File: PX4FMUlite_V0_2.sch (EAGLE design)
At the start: 156 parts, among them J201 DF13C-6P-1.25V, J202 DF13C-6P-1.25V, J203 DF13C-6P-1.25V, J204 DF13C-6P-1.25V, J301 47346-0001, J302 DF13C-4P-1.25V, J401 DF13C-4P-1.25V, J403 DF13C-7P-1.25V, J404 DF13C-5P-1.25V, J405 DF13C-4P-1.25V, J702 DF13C-3P-1.25V, J801 JST-ZH-3, M3_MOUNT1101 MOUNT-HOLE3.1MM, M3_MOUNT1102 MOUNT-HOLE3.1MM, M3_MOUNT1103 MOUNT-HOLE3.1MM, M3_MOUNT1104 MOUNT-HOLE3.1MM, U1 MPU-6000QFN-24, U101 STM32F4X7VX, U102 FM25V01, U401 MAX3051, U701 TCA62724FMG, U703 LRTB GFTG-T7AW-1+V7A7-29+R5T9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, U903 74LVC2G240, X101 3.2x2.5 mm / 24 MHz / 15 ppm

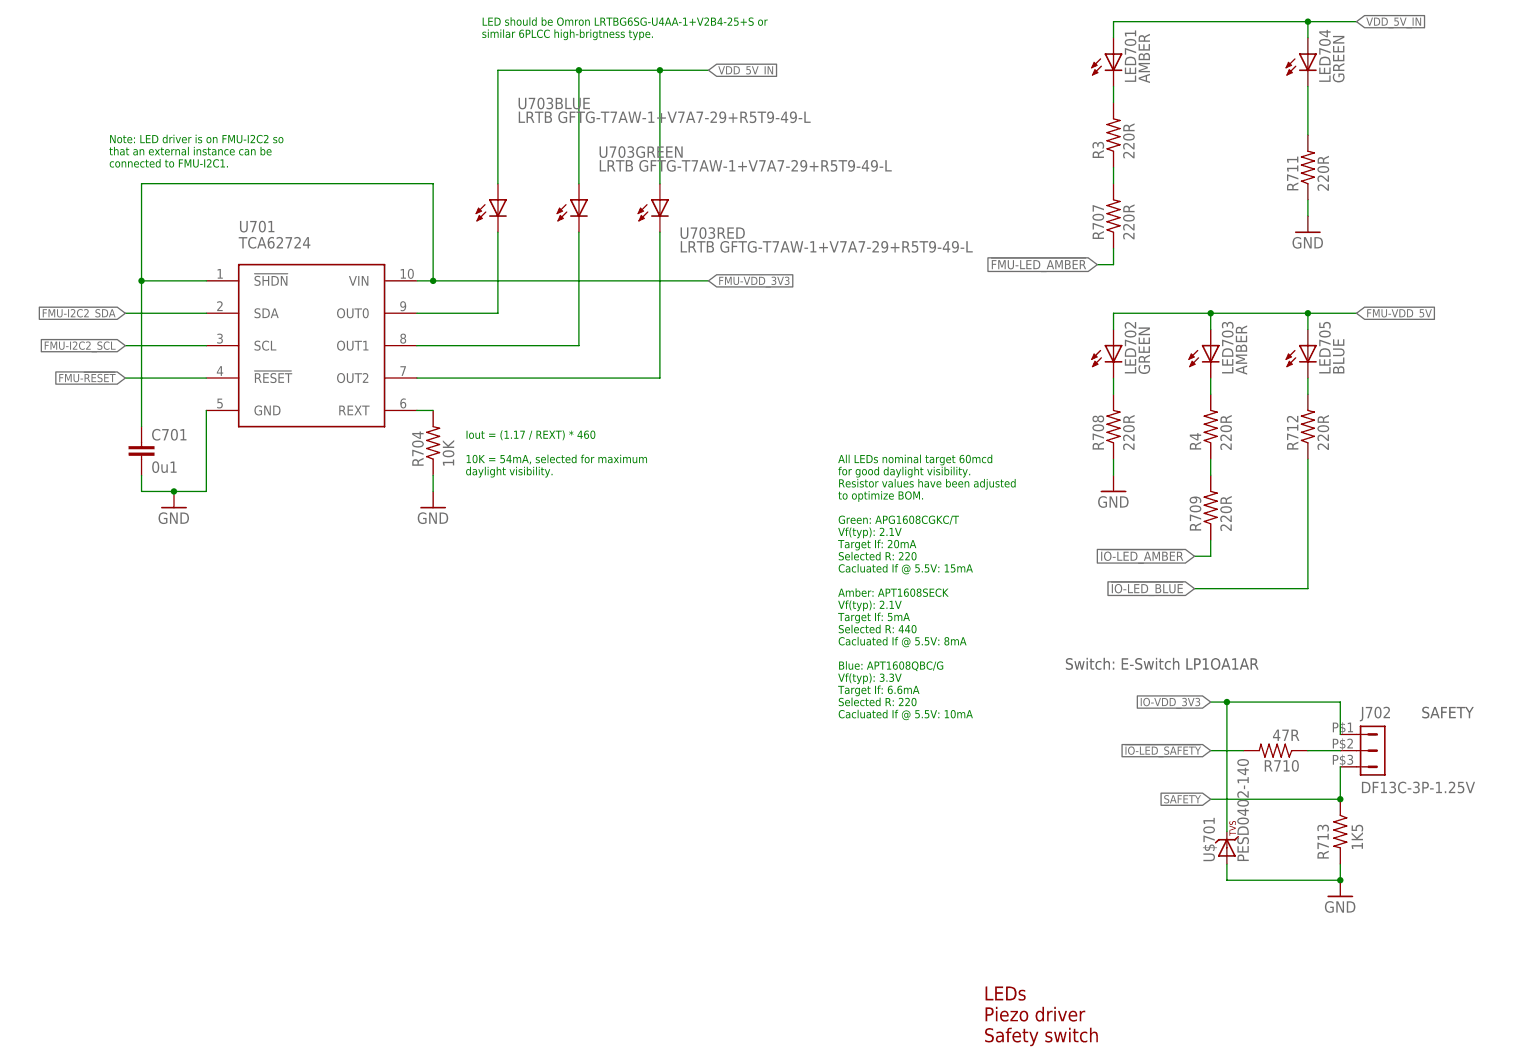
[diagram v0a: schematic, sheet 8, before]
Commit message: Added V0_2 because V0_1 would not save
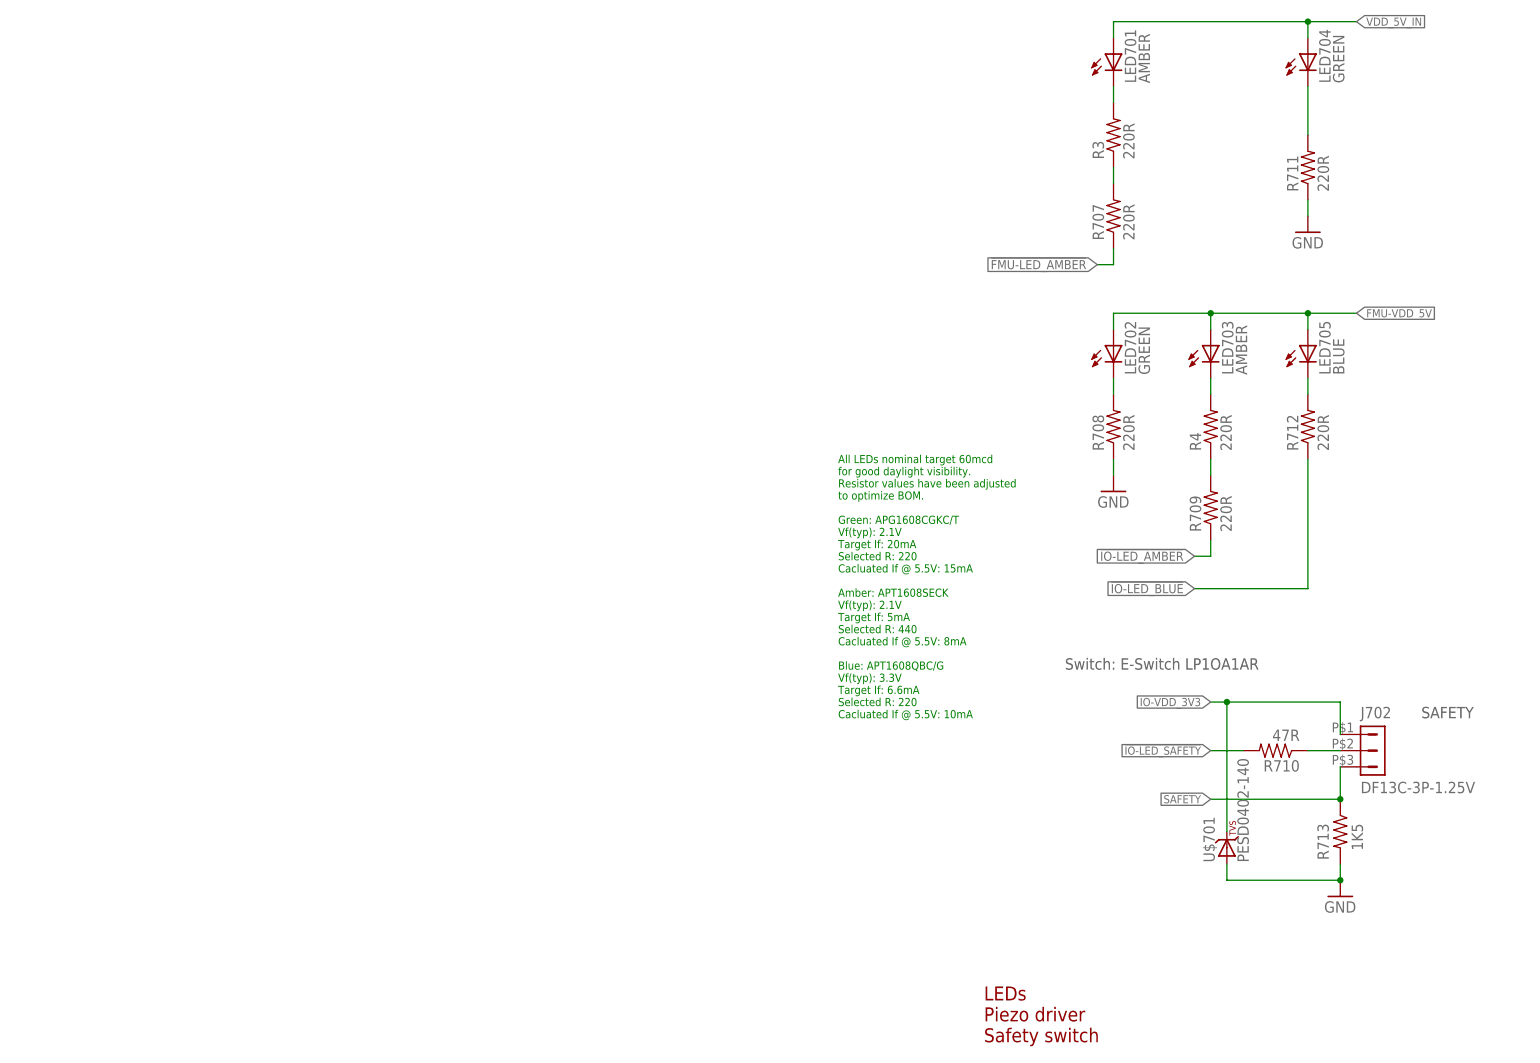
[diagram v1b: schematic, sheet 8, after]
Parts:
- removed C701: 0u1, pixhawk2:CAP0402
- removed L601, L602: KNH16C104DA5TS, pixhawk2:KNH16C104DA5TS
- removed R604, R605: 10K/0.1%, pixhawk2:RESISTOR0402-RES
- removed R704: 10K, pixhawk2:RESISTOR0402-RES
- removed U701: TCA62724FMG, pixhawk2:TCA62724FMG
- removed U703: LRTB GFTG-T7AW-1+V7A7-29+R5T9-49-L, pixhawk2:RGB-LED6-PLCC
- added U$2: LSM303D, PX4FMUlite_V0_1:LSM303D
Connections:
- removed net BATT_CURRENT_SENS: R604.1
- removed net BATT_VOLTAGE_SENS: R605.1
- removed net BATT_VOLTAGE_SENS_PROT: L602.P$1
- removed net N$102: L602.P$2, R605.2
- removed net N$103: L601.P$2, R604.2
- removed net N$21: L601.P$1
- removed net N$95: R704.2, U701.REXT
- removed net RGB_LED_14: U701.OUT2, U703RED.C
- removed net RGB_LED_3: U701.OUT0, U703BLUE.C
- removed net RGB_LED_4: U701.OUT1, U703GREEN.C
- net !ACCEL_MAG_CS: now also U$2.CS
- net ACCEL_DRDY: now also U$2.INT1
- net FMU-!RESET: no longer U701.!RESET
- net FMU-I2C2_SCL: no longer U701.SCL
- net FMU-I2C2_SDA: no longer U701.SDA
- net FMU-VDD_3V3: no longer C701.1, U701.!SHDN, U701.VIN
- net GNDX: now also U$2.GND@1, U$2.GND@2, U$2.GND@3, U$2.GND@4, U$2.RSRV; no longer C701.2, L601.P$3, L602.P$3, R704.1, U701.GND
- net MAG_DRDY: now also U$2.INT2
- net N$10: now also U$2.SETC
- net N$17: now also U$2.SETP
- net N$6: now also U$2.C1
- net SPI_INT_MISO: now also U$2.SDO/SA0
- net SPI_INT_MOSI: now also U$2.SDA/SDI/SDO
- net SPI_INT_SCK: now also U$2.SCL/SPC
- net VDD_3V3_SENSORS: now also U$2.VDD, U$2.VDD_IO
- net VDD_5V_IN: no longer U703BLUE.A, U703GREEN.A, U703RED.A
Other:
- note removed: "Iout = (1.17 / REXT) * 460 10K = 54mA, selected for maximum daylight visibility."
- note removed: "LED should be Omron LRTBG6SG-U4AA-1+V2B4-25+S or similar 6PLCC high-brigtness type."
- note removed: "Note: LED driver is on FMU-I2C2 so that an external instance can be connected to FMU-I2C1."

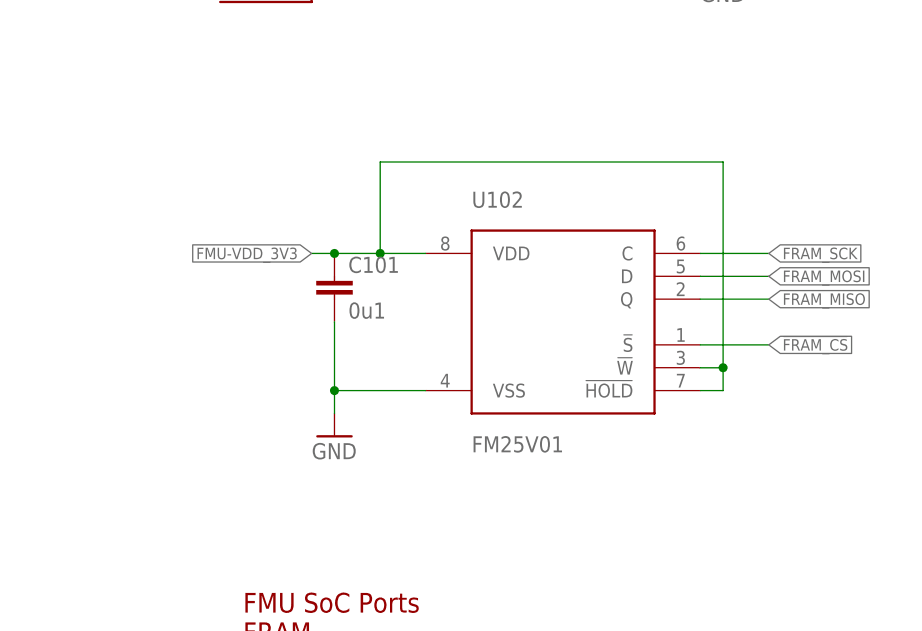
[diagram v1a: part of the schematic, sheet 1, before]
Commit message: Changed to winbond W25Q64 64mbit flash in 5*6 8WSON
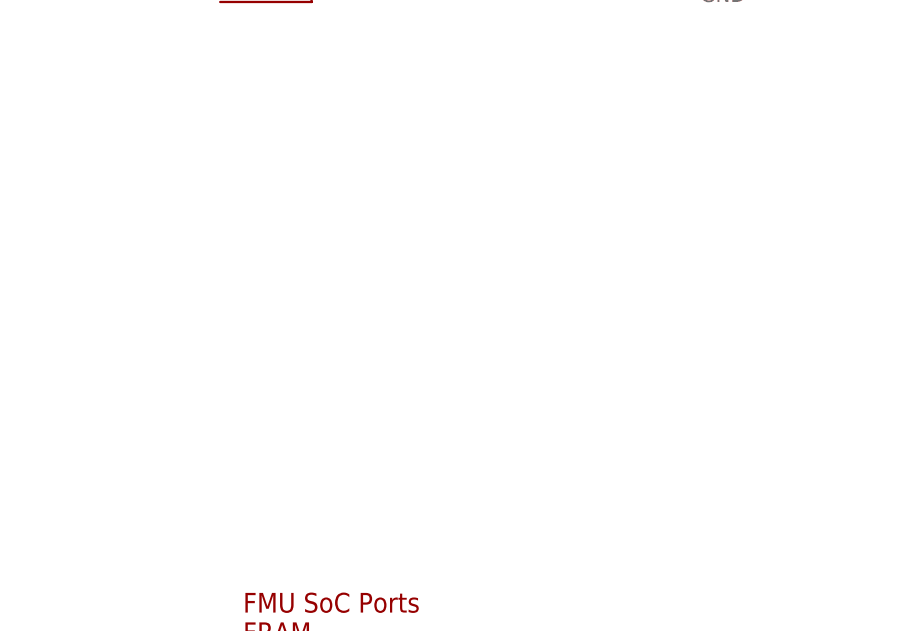
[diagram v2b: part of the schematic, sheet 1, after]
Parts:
- removed C101: 0u1, pixhawk2:CAP0402
- removed U102: FM25V01, pixhawk2:FM25V01
- added U$3: W25Q64FV, PX4lite:W25Q64FV
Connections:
- net !FRAM_CS: no longer U102.!S
- net FMU-VDD_3V3: no longer C101.1, U102.!HOLD, U102.!W, U102.VDD
- net FRAM_MISO: no longer U102.Q
- net FRAM_MOSI: no longer U102.D
- net FRAM_SCK: no longer U102.C
- net GNDX: no longer C101.2, U102.VSS
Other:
- note removed: "Stuff option 2: L3GD20H (replacement gyro)"
- note removed: "Stuff option 4: onboard accel/mag"
- note removed: "Valid stuff option combos: 1 + 4 2 + 4 3 only DO NOT stuff 1 + 2 at the same time DO NOT stuff 3 with any of 1, 2 or 4"
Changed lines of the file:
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@@
 <attribute name="PARTNO" value="RC0402FR-071K5L"/>
-</part>
-<part name="GND15" library="pixhawk2" deviceset="GND" device=""/>
-<part name="U102" library="pixhawk2" deviceset="FM25V01" device="">
-<attribute name="PARTNO" value="FM25V01-G"/>
-</part>
-<part name="C101" library="pixhawk2" deviceset="CAP" device="0402" value="0u1">
-<attribute name="PARTNO" value="CC0402ZRY5V7BB104"/>
 </part>
 <part name="J302" library="con-hirose-df13" deviceset="DF13-4P-1.25" device="V" value="DF13C-4P-1.25V">
@@
 <part name="U1" library="SparkFun-Sensors" deviceset="MPU-6000" device="QFN-24"/>
 <part name="U$2" library="PX4FMUlite_V0_1" deviceset="LSM303D" device=""/>
+<part name="U$3" library="PX4lite" deviceset="W25Q64FV" device=""/>
 </parts>
 <sheets>
@@
 <instance part="U101" gate="PORTE_H" x="165.1" y="129.54" rot="MR0"/>
 <instance part="U101" gate="OSC" x="165.1" y="91.44"/>
-<instance part="GND15" gate="1" x="172.72" y="38.1"/>
-<instance part="U102" gate="G$1" x="198.12" y="50.8">
-<attribute name="PARTNO" x="198.12" y="50.8" size="1.778" layer="96" display="off"/>
-</instance>
-<instance part="C101" gate="G$1" x="172.72" y="53.34">
-<attribute name="PARTNO" x="172.72" y="53.34" size="1.778" layer="96" display="off"/>
-</instance>
 <instance part="R101" gate="G$1" x="60.96" y="132.08">
 <attribute name="PARTNO" x="60.96" y="132.08" size="1.778" layer="96" display="off"/>
@@
 <pinref part="X101" gate="G$1" pin="NC_2"/>
 </segment>
-<segment>
-<pinref part="U102" gate="G$1" pin="VSS"/>
-<pinref part="GND15" gate="1" pin="GND"/>
-<wire x1="182.88" y1="43.18" x2="172.72" y2="43.18" width="0.1524" layer="91"/>
-<wire x1="172.72" y1="43.18" x2="172.72" y2="40.64" width="0.1524" layer="91"/>
-<pinref part="C101" gate="G$1" pin="2"/>
-<wire x1="172.72" y1="43.18" x2="172.72" y2="50.8" width="0.1524" layer="91"/>
-<junction x="172.72" y="43.18"/>
-</segment>
 </net>
 <net name="CAN1_RX" class="0">
@@
 </segment>
 </net>
-<net name="FMU-VDD_3V3" class="1">
-<segment>
-<pinref part="U102" gate="G$1" pin="VDD"/>
-<wire x1="182.88" y1="58.42" x2="177.8" y2="58.42" width="0.1524" layer="91"/>
-<label x="170.18" y="58.42" size="1.27" layer="95" rot="R180" xref="yes"/>
-<pinref part="C101" gate="G$1" pin="1"/>
-<wire x1="177.8" y1="58.42" x2="172.72" y2="58.42" width="0.1524" layer="91"/>
-<wire x1="172.72" y1="58.42" x2="170.18" y2="58.42" width="0.1524" layer="91"/>
-<junction x="172.72" y="58.42"/>
-<pinref part="U102" gate="G$1" pin="!HOLD"/>
-<wire x1="213.36" y1="43.18" x2="215.9" y2="43.18" width="0.1524" layer="91"/>
-<wire x1="215.9" y1="43.18" x2="215.9" y2="45.72" width="0.1524" layer="91"/>
-<wire x1="215.9" y1="45.72" x2="215.9" y2="68.58" width="0.1524" layer="91"/>
-<wire x1="215.9" y1="68.58" x2="177.8" y2="68.58" width="0.1524" layer="91"/>
-<wire x1="177.8" y1="68.58" x2="177.8" y2="58.42" width="0.1524" layer="91"/>
-<junction x="177.8" y="58.42"/>
-<pinref part="U102" gate="G$1" pin="!W"/>
-<wire x1="213.36" y1="45.72" x2="215.9" y2="45.72" width="0.1524" layer="91"/>
-<junction x="215.9" y="45.72"/>
-</segment>
-</net>
 <net name="!FRAM_CS" class="0">
-<segment>
-<pinref part="U102" gate="G$1" pin="!S"/>
-<wire x1="213.36" y1="48.26" x2="220.98" y2="48.26" width="0.1524" layer="91"/>
-<label x="220.98" y="48.26" size="1.27" layer="95" xref="yes"/>
-</segment>
 <segment>
 <pinref part="U101" gate="PORTD_H" pin="PD10"/>
@@
 <net name="FRAM_SCK" class="0">
 <segment>
-<pinref part="U102" gate="G$1" pin="C"/>
-<wire x1="213.36" y1="58.42" x2="220.98" y2="58.42" width="0.1524" layer="91"/>
-<label x="220.98" y="58.42" size="1.27" layer="95" xref="yes"/>
-</segment>
-<segment>
 <pinref part="U101" gate="PORTB_H" pin="PB13"/>
 <wire x1="33.02" y1="68.58" x2="38.1" y2="68.58" width="0.1524" layer="91"/>
@@
 <net name="FRAM_MOSI" class="0">
 <segment>
-<pinref part="U102" gate="G$1" pin="D"/>
-<wire x1="213.36" y1="55.88" x2="220.98" y2="55.88" width="0.1524" layer="91"/>
-<label x="220.98" y="55.88" size="1.27" layer="95" xref="yes"/>
-</segment>
-<segment>
 <pinref part="U101" gate="PORTB_H" pin="PB15"/>
 <wire x1="33.02" y1="63.5" x2="38.1" y2="63.5" width="0.1524" layer="91"/>
@@
 </net>
 <net name="FRAM_MISO" class="0">
-<segment>
-<pinref part="U102" gate="G$1" pin="Q"/>
-<wire x1="213.36" y1="53.34" x2="220.98" y2="53.34" width="0.1524" layer="91"/>
-<label x="220.98" y="53.34" size="1.27" layer="95" xref="yes"/>
-</segment>
 <segment>
 <pinref part="U101" gate="PORTB_H" pin="PB14"/>
@@
 <attribute name="PARTNO" x="53.34" y="134.62" size="1.778" layer="96" display="off"/>
 </instance>
+<instance part="U$3" gate="G$1" x="109.22" y="76.2"/>
 </instances>
 <busses>
@@
 <wire x1="248.92" y1="33.02" x2="185.42" y2="33.02" width="0.1524" layer="94" style="dashdot"/>
 <wire x1="185.42" y1="33.02" x2="185.42" y2="68.58" width="0.1524" layer="94" style="dashdot"/>
-<text x="6.35" y="34.29" size="1.778" layer="94">Stuff option 2: L3GD20H (replacement gyro)</text>
 <text x="187.198" y="34.036" size="1.778" layer="94">Stuff option 3: offboard gyro/accel/mag</text>
 <wire x1="127" y1="165.1" x2="254" y2="165.1" width="0.1524" layer="94" style="dashdot"/>
 <wire x1="254" y1="165.1" x2="254" y2="101.6" width="0.1524" layer="94" style="dashdot"/>
 <wire x1="254" y1="101.6" x2="127" y2="101.6" width="0.1524" layer="94" style="dashdot"/>
-<text x="128.016" y="102.616" size="1.778" layer="94">Stuff option 4: onboard accel/mag</text>
-<text x="101.6" y="10.16" size="1.778" layer="94">Valid stuff option combos:
-  1 + 4
-  2 + 4
-  3 only
-DO NOT stuff 1 + 2 at the same time
-DO NOT stuff 3 with any of 1, 2 or 4</text>
 <text x="22.86" y="111.76" size="1.778" layer="91">THIS IS A SPARKFUN LIBRARY PART USED FOR REFERENCE ONLY.
 MUST BE REPLACED WITH OWN LIBRARY PART</text>

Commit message: Test positioning
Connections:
- new net GND: U$3.GND
- net FMU-VDD_3V3: now also U$3.VCC
- net SDIO_CK: now also U$3.CLK
- net SDIO_CMD: now also U$3.!CS
- net SDIO_D0: now also U$3.DI/IO0
- net SDIO_D1: now also U$3.DO/IO1
- net SDIO_D2: now also U$3.!WP!/IO2
- net SDIO_D3: now also U$3.!HOLD!/IO3
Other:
- moved on the sheet: U$3
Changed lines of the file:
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@@
 <part name="U$2" library="PX4FMUlite_V0_1" deviceset="LSM303D" device=""/>
 <part name="U$3" library="PX4lite" deviceset="W25Q64FV" device=""/>
+<part name="GND12" library="pixhawk2" deviceset="GND" device=""/>
 </parts>
 <sheets>
@@
 <attribute name="PARTNO" x="53.34" y="134.62" size="1.778" layer="96" display="off"/>
 </instance>
-<instance part="U$3" gate="G$1" x="109.22" y="76.2"/>
+<instance part="U$3" gate="G$1" x="81.28" y="50.8"/>
+<instance part="GND12" gate="1" x="76.2" y="27.94"/>
 </instances>
 <busses>
@@
 <junction x="149.86" y="152.4"/>
 </segment>
+<segment>
+<wire x1="68.58" y1="71.12" x2="76.2" y2="71.12" width="0.1524" layer="91"/>
+<pinref part="U$3" gate="G$1" pin="VCC"/>
+<wire x1="76.2" y1="71.12" x2="76.2" y2="66.04" width="0.1524" layer="91"/>
+<label x="68.58" y="71.12" size="1.778" layer="95" rot="R180"/>
+</segment>
 </net>
 <net name="OTG_DM1" class="0">
@@
 </segment>
 </net>
-<net name="N$4" class="1">
-<segment>
-<wire x1="81.28" y1="71.12" x2="78.74" y2="71.12" width="0.1524" layer="91"/>
-</segment>
-</net>
+<net name="SDIO_D0" class="0">
+<segment>
+<pinref part="U$3" gate="G$1" pin="DI/IO0"/>
+<wire x1="96.52" y1="50.8" x2="109.22" y2="50.8" width="0.1524" layer="91"/>
+<label x="109.22" y="50.8" size="1.778" layer="95"/>
+</segment>
+</net>
+<net name="SDIO_D1" class="0">
+<segment>
+<pinref part="U$3" gate="G$1" pin="DO/IO1"/>
+<wire x1="96.52" y1="48.26" x2="109.22" y2="48.26" width="0.1524" layer="91"/>
+<label x="109.22" y="48.26" size="1.778" layer="95"/>
+</segment>
+</net>
+<net name="SDIO_D2" class="0">
+<segment>
+<pinref part="U$3" gate="G$1" pin="!WP!/IO2"/>
+<wire x1="96.52" y1="45.72" x2="109.22" y2="45.72" width="0.1524" layer="91"/>
+<label x="109.22" y="45.72" size="1.778" layer="95"/>
+</segment>
+</net>
+<net name="SDIO_D3" class="0">
+<segment>
+<pinref part="U$3" gate="G$1" pin="!HOLD!/IO3"/>
+<wire x1="96.52" y1="43.18" x2="109.22" y2="43.18" width="0.1524" layer="91"/>
+<label x="109.22" y="43.18" size="1.778" layer="95"/>
+</segment>
+</net>
+<net name="SDIO_CMD" class="0">
+<segment>
+<pinref part="U$3" gate="G$1" pin="!CS"/>
+<wire x1="96.52" y1="55.88" x2="109.22" y2="55.88" width="0.1524" layer="91"/>
+<label x="109.22" y="55.88" size="1.778" layer="95"/>
+</segment>
+</net>
+<net name="SDIO_CK" class="0">
+<segment>
+<pinref part="U$3" gate="G$1" pin="CLK"/>
+<wire x1="96.52" y1="58.42" x2="109.22" y2="58.42" width="0.1524" layer="91"/>
+<label x="109.22" y="58.42" size="1.778" layer="95"/>
+</segment>
+</net>
+<net name="GND" class="0">
+<segment>
+<pinref part="U$3" gate="G$1" pin="GND"/>
+<pinref part="GND12" gate="1" pin="GND"/>
+<wire x1="76.2" y1="35.56" x2="76.2" y2="30.48" width="0.1524" layer="91"/>
+</segment>
+</net>
